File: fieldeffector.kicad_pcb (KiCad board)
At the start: 2 copper layers, 88.2 x 48 mm, 34 parts, among them J1 Conn_01x02, J10 Conn_01x02, J2 Conn_01x02, J3 Conn_01x02, J4 Conn_01x02, J5 Conn_01x02, J6 Conn_01x02, J7 Conn_01x02, J8 Conn_01x02, J9 Conn_01x02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

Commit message: add system ground
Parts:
- H3: value MountingHole -> MountingHole_Pad; footprint MountingHole:MountingHole_3.2mm_M3 -> MountingHole:MountingHole_3.2mm_M3_Pad_Via
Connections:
- H3 pad 1: (no net) -> Net-(H3-Pad1)
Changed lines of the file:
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@@
     (zones 0)
     (modules 34)
-    (nets 20)
+    (nets 21)
   )
   (page A4)
@@
     (solder_mask_min_width 0.25)
     (aux_axis_origin 73.4 88.065)
-    (grid_origin 149.2 120.265)
+    (grid_origin 77.9 131.315)
     (visible_elements FFFFF77F)
     (pcbplotparams
@@
       (drillshape 0)
       (scaleselection 1)
-      (outputdirectory ""))
+      (outputdirectory "gerber/"))
   )
   (net 0 "")
@@
   (net 18 "Net-(J7-Pad2)")
   (net 19 "Net-(U1-Pad1)")
+  (net 20 "Net-(H3-Pad1)")
   (net_class Default "This is the default net class."
     (clearance 0.2)
@@
     (add_net "Net-(D3-Pad2)")
     (add_net "Net-(D4-Pad2)")
+    (add_net "Net-(H3-Pad1)")
     (add_net "Net-(J10-Pad2)")
     (add_net "Net-(J7-Pad2)")
@@
     (uvia_drill 0.1)
   )
+  (module MountingHole:MountingHole_3.2mm_M3_Pad_Via (layer F.Cu)
+    (at 153.65 128.065)
+    (descr "Mounting Hole 3.2mm, M3")
+    (tags "mounting hole 3.2mm m3")
+    (attr virtual)
+    (fp_text reference H3 (at 0 -4.2) (layer F.SilkS)
+      (effects (font (size 1 1) (thickness 0.15)))
+    )
+    (fp_text value MountingHole_Pad (at 0 4.2) (layer F.Fab)
+      (effects (font (size 1 1) (thickness 0.15)))
+    )
+    (fp_text user %R (at 0.3 0) (layer F.Fab)
+      (effects (font (size 1 1) (thickness 0.15)))
+    )
+    (fp_circle (center 0 0) (end 3.2 0) (layer Cmts.User) (width 0.15))
+    (fp_circle (center 0 0) (end 3.45 0) (layer F.CrtYd) (width 0.05))
+    (pad 1 thru_hole circle (at 0 0) (size 6.4 6.4) (drill 3.2) (layers *.Cu *.Mask)
+      (net 20 "Net-(H3-Pad1)"))
+    (pad 1 thru_hole circle (at 2.4 0) (size 0.8 0.8) (drill 0.5) (layers *.Cu *.Mask)
+      (net 20 "Net-(H3-Pad1)"))
+    (pad 1 thru_hole circle (at 1.697056 1.697056) (size 0.8 0.8) (drill 0.5) (layers *.Cu *.Mask)
+      (net 20 "Net-(H3-Pad1)"))
+    (pad 1 thru_hole circle (at 0 2.4) (size 0.8 0.8) (drill 0.5) (layers *.Cu *.Mask)
+      (net 20 "Net-(H3-Pad1)"))
+    (pad 1 thru_hole circle (at -1.697056 1.697056) (size 0.8 0.8) (drill 0.5) (layers *.Cu *.Mask)
+      (net 20 "Net-(H3-Pad1)"))
+    (pad 1 thru_hole circle (at -2.4 0) (size 0.8 0.8) (drill 0.5) (layers *.Cu *.Mask)
+      (net 20 "Net-(H3-Pad1)"))
+    (pad 1 thru_hole circle (at -1.697056 -1.697056) (size 0.8 0.8) (drill 0.5) (layers *.Cu *.Mask)
+      (net 20 "Net-(H3-Pad1)"))
+    (pad 1 thru_hole circle (at 0 -2.4) (size 0.8 0.8) (drill 0.5) (layers *.Cu *.Mask)
+      (net 20 "Net-(H3-Pad1)"))
+    (pad 1 thru_hole circle (at 1.697056 -1.697056) (size 0.8 0.8) (drill 0.5) (layers *.Cu *.Mask)
+      (net 20 "Net-(H3-Pad1)"))
+  )
   (module MountingHole:MountingHole_3.2mm_M3 (layer F.Cu)
     (at 153.65 88.065)
@@
       (effects (font (size 1 1) (thickness 0.15)))
     )
-    (pad 1 np_thru_hole circle (at 0 0) (size 3.2 3.2) (drill 3.2) (layers *.Cu *.Mask))
-  )
-  (module MountingHole:MountingHole_3.2mm_M3 (layer F.Cu)
-    (at 153.65 128.065)
-    (descr "Mounting Hole 3.2mm, no annular, M3")
-    (tags "mounting hole 3.2mm no annular m3")
-    (attr virtual)
-    (fp_text reference H3 (at 0 -4.2) (layer F.SilkS)
-      (effects (font (size 1 1) (thickness 0.15)))
-    )
-    (fp_text value MountingHole (at 0 4.2) (layer F.Fab)
-      (effects (font (size 1 1) (thickness 0.15)))
-    )
-    (fp_text user %R (at 0.3 0) (layer F.Fab)
-      (effects (font (size 1 1) (thickness 0.15)))
-    )
-    (fp_circle (center 0 0) (end 3.2 0) (layer Cmts.User) (width 0.15))
-    (fp_circle (center 0 0) (end 3.45 0) (layer F.CrtYd) (width 0.05))
     (pad 1 np_thru_hole circle (at 0 0) (size 3.2 3.2) (drill 3.2) (layers *.Cu *.Mask))
   )
@@
     (polygon
       (pts
-        (xy 84.6 115.065) (xy 84.6 101.465) (xy 77.8 101.465) (xy 77.8 129.965) (xy 155.8 129.965)
-        (xy 155.8 115.065)
+        (xy 84.65 115.065) (xy 84.65 101.565) (xy 77.15 101.565) (xy 77.15 131.315) (xy 156.9 131.315)
+        (xy 156.9 115.065)
       )
     )

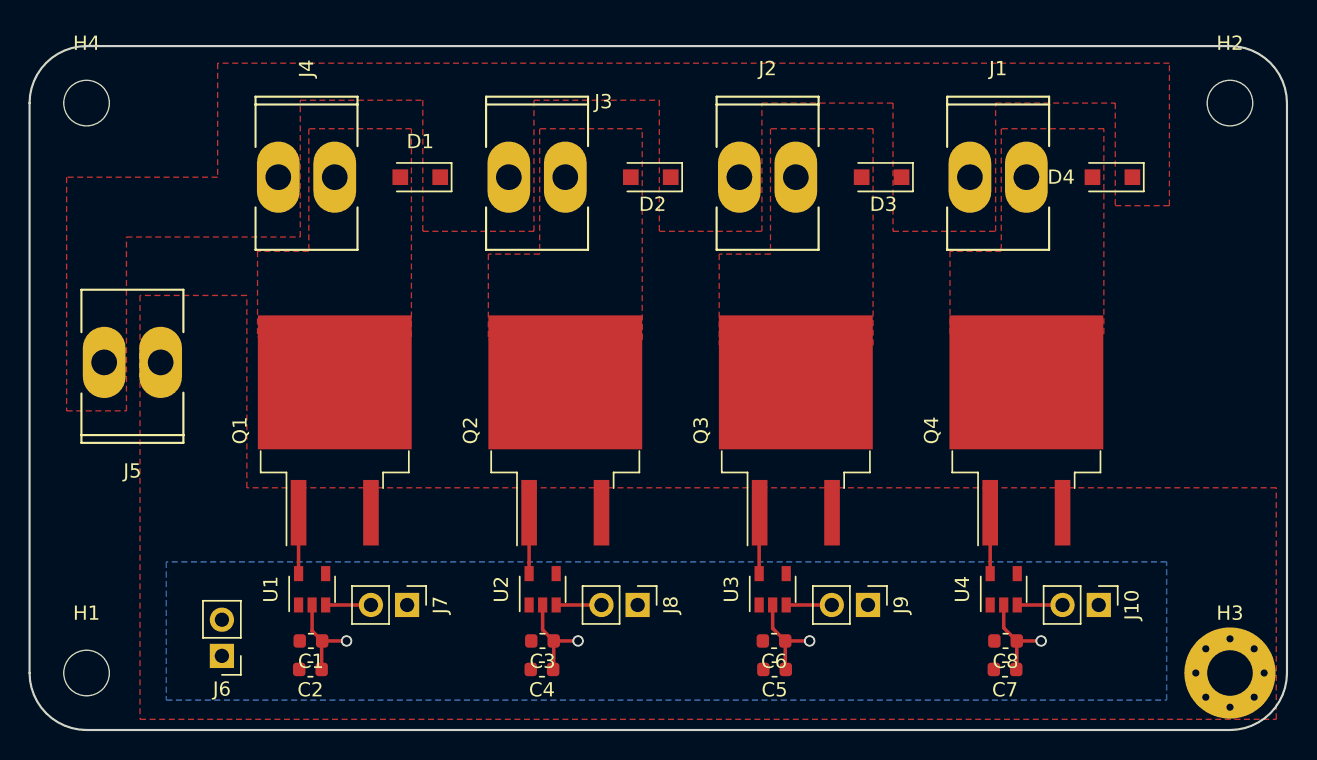
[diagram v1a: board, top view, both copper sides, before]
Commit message: fixed diode pads
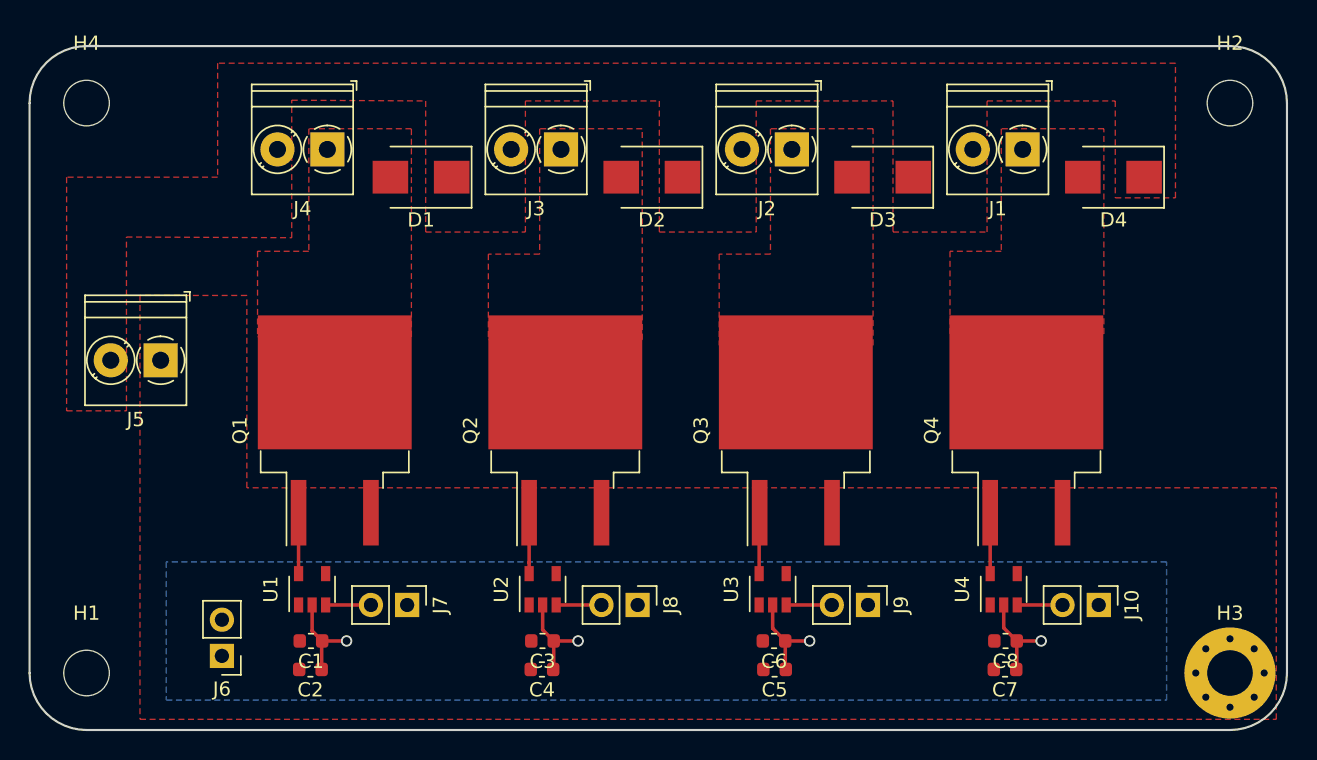
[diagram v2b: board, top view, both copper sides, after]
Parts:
- D1, D2, D3, D4: footprint Diode_SMD:D_SOD-123F -> Diode_SMD:D_SMB
- J1, J2, J3, J4, J5: footprint Sockets_MOLEX_KK-System:Socket_MOLEX-KK-RM3-96mm_Lock_2pin_straight -> TerminalBlock_Phoenix:TerminalBlock_Phoenix_PT-1,5-2-3.5-H_1x02_P3.50mm_Horizontal
- moved J1 2.60 mm to (139.1, 91.3), turned to 180 degrees
- moved J2 2.59 mm to (122.9, 91.3), turned to 180 degrees
- moved J3 2.57 mm to (106.7, 91.3), turned to 180 degrees
- moved J4 2.44 mm to (90.3, 91.3), turned to 180 degrees
- moved J5 1.99 mm to (78.6, 106.1)
- moved D3 0.08 mm to (129.3, 93.3)
- moved D2 0.08 mm to (113.1, 93.3)
- moved D4 0.07 mm to (145.5, 93.3)
- moved D1 0.06 mm to (96.9, 93.3)
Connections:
- H3 pad 1: Net-(H3-Pad1) -> GND
- J1 pad 1: +48V -> Net-(D4-Pad2)
- J1 pad 2: Net-(D4-Pad2) -> +48V
- J2 pad 1: +48V -> Net-(D3-Pad2)
- J2 pad 2: Net-(D3-Pad2) -> +48V
- J3 pad 1: +48V -> Net-(D2-Pad2)
- J3 pad 2: Net-(D2-Pad2) -> +48V
- J4 pad 1: +48V -> Net-(D1-Pad2)
- J4 pad 2: Net-(D1-Pad2) -> +48V

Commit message: update
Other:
- board text added: "Fieldeffector"
- board text added: "Spiderbox"
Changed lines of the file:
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@@
   (general
     (thickness 1.6)
-    (drawings 8)
+    (drawings 14)
     (tracks 33)
     (zones 0)
@@
     (solder_mask_min_width 0.25)
     (aux_axis_origin 73.4 88.065)
-    (grid_origin 96.625 93.265)
+    (grid_origin 166.65 110.265)
     (visible_elements FFFFFF7F)
     (pcbplotparams
@@
     )
   )
+  (gr_circle (center 151.05 104.074381) (end 150.368033 104.474381) (layer F.SilkS) (width 0.15))
+  (gr_circle (center 151.05 106.346967) (end 150.55 105.346967) (layer F.SilkS) (width 0.15))
+  (gr_circle (center 151.05 111.255619) (end 151.45 111.937586) (layer F.SilkS) (width 0.15))
+  (gr_circle (center 151.05 108.983033) (end 151.55 109.983033) (layer F.SilkS) (width 0.15))
+  (gr_text "Fieldeffector\n\n" (at 154.45 107.665 90) (layer F.SilkS)
+    (effects (font (size 1 1) (thickness 0.15)))
+  )
+  (gr_text "Spiderbox\n" (at 148.45 107.465 90) (layer F.SilkS)
+    (effects (font (size 1 1) (thickness 0.15)))
+  )
   (gr_line (start 153.65 132.065) (end 73.4 132.065) (layer Edge.Cuts) (width 0.15))
